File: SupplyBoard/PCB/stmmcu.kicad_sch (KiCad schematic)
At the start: 15 parts, among them J3 Conn_01x04, SW2 RESET, SW3 SW_SPDT, U1 STM32L031F6Px, Y1 16Mhz

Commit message: Supply Board & Folder Organization
Reorganization of the power supply board components, simplifying the layout to facilitate future debugging and reorganizing some folders and documents, as well as adding the power supply board schematic; in supply board only need to make the routing
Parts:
- Y1: footprint Crystal:Crystal_SMD_0603-4Pin_6.0x3.5mm_HandSoldering -> Crystal:Crystal_SMD_2016-4Pin_2.0x1.6mm
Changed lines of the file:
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@@
 			)
 		)
-		(property "Footprint" "Crystal:Crystal_SMD_0603-4Pin_6.0x3.5mm_HandSoldering"
+		(property "Footprint" "Crystal:Crystal_SMD_2016-4Pin_2.0x1.6mm"
 			(at 40.64 76.2 0)
 			(effects

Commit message: Start the S&CBoard
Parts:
- removed C2, C5: 9pF, Capacitor_SMD:C_0805_2012Metric_Pad1.18x1.45mm_HandSolder, symbol Device:C_Small
- removed Y1: 16Mhz, Crystal:Crystal_SMD_2016-4Pin_2.0x1.6mm, symbol Device:Crystal_GND24
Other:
- note removed: "Crystal Osc"
- moved on the sheet: C3, C4

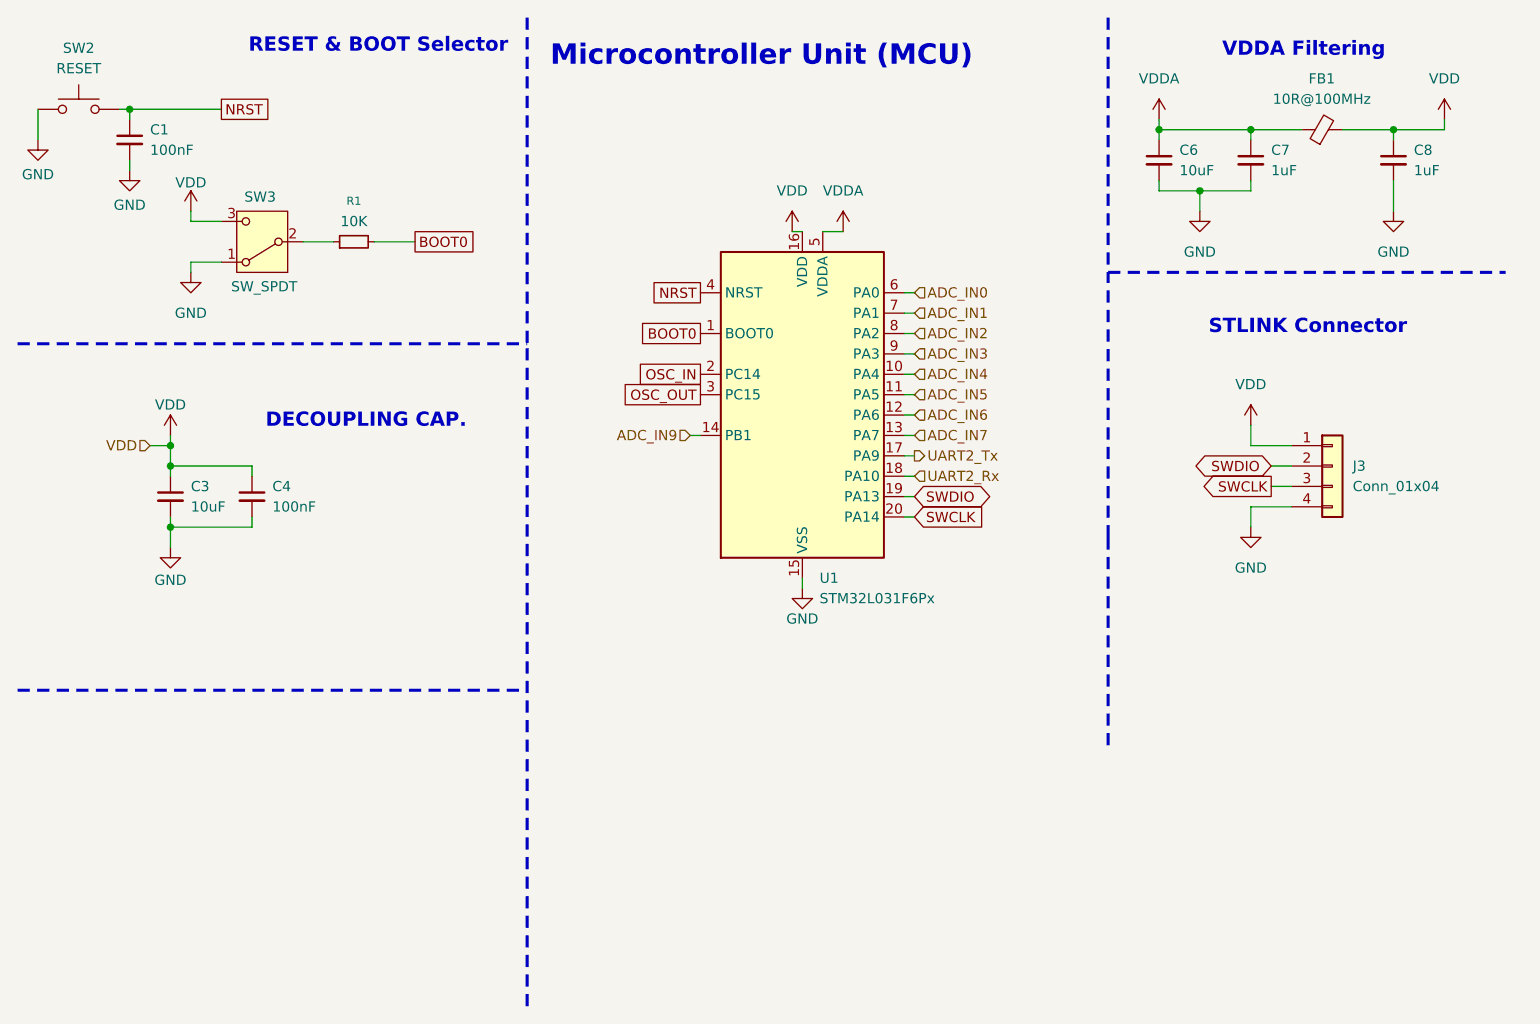
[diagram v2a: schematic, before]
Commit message: Supply & Coms-Sensor Board
la organizacion de los componentes presentes en las placas, se quedaran de esa manera, se espera que en la serigrafia se incluyan los logos de los patrocinadores, ademas se incluyo la carpeta 3D la cual contiene modelos en 3D de las dos placas, con serigrafia y componentes incluidos y ya
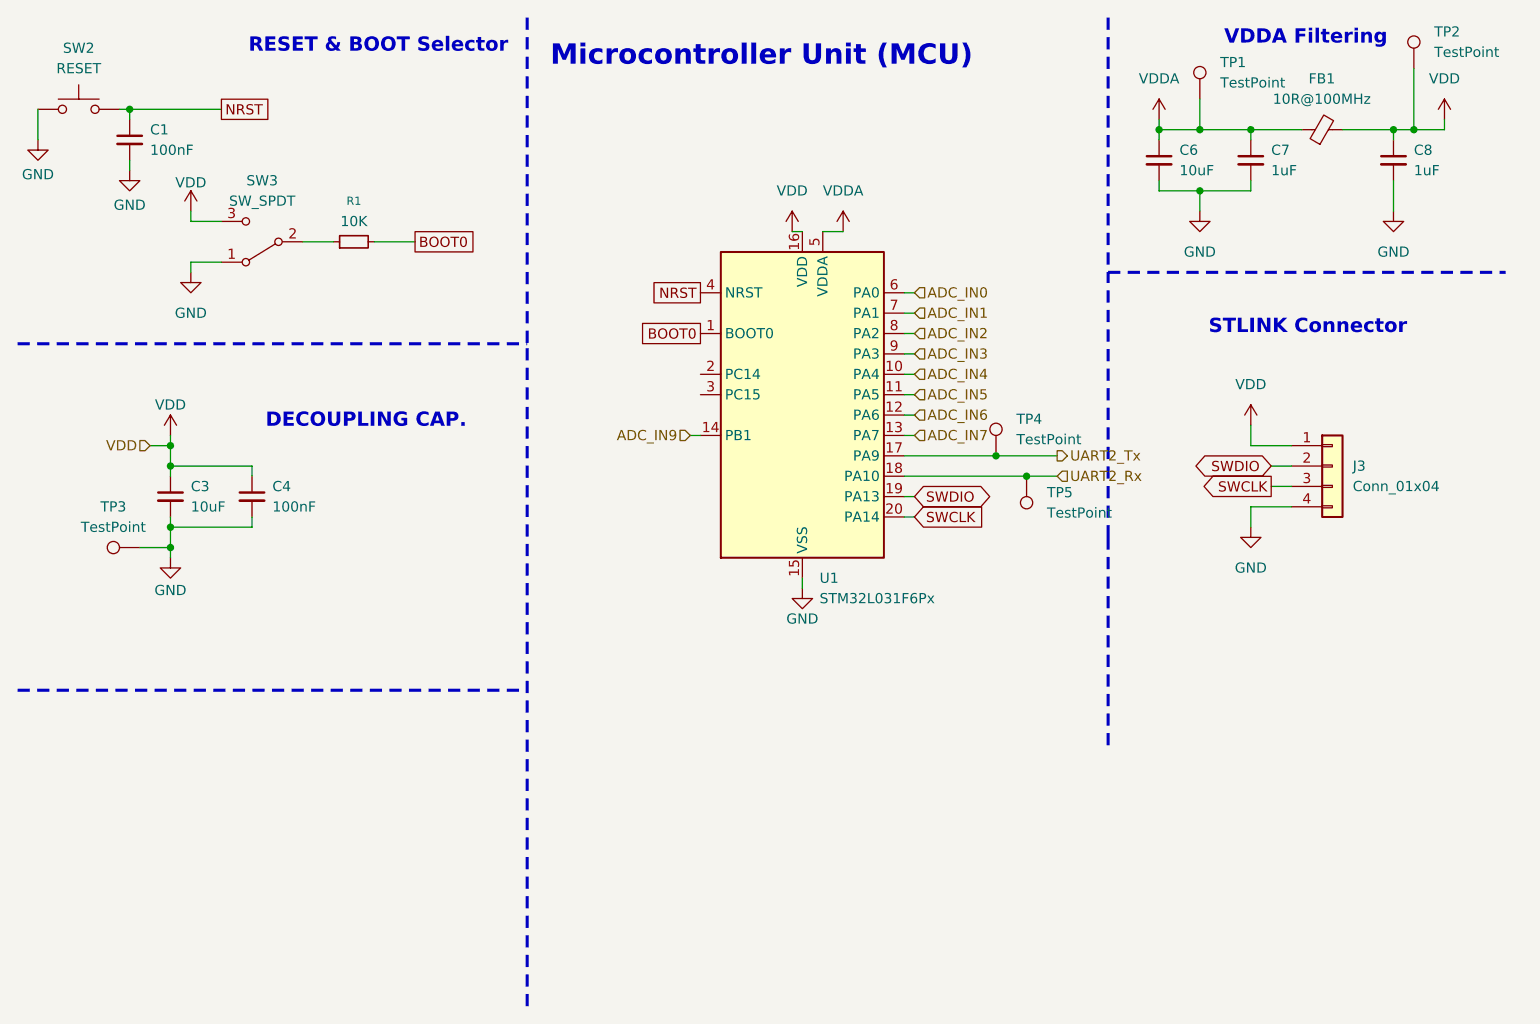
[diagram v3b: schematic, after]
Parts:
- removed SW3: SW_SPDT, Connector_PinHeader_2.54mm:PinHeader_1x03_P2.54mm_Vertical, symbol Switch:SW_SPDT
- added SW3: SW_SPDT, Button_Switch_SMD:SW_SPDT_Shouhan_MSK12C02, symbol CompVuelo:SW_SPDT
- added TP1, TP2, TP3, TP4, TP5: TestPoint, TestPoint:TestPoint_Pad_D1.5mm, symbol Connector:TestPoint
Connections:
- net GND: now also SW3.1, TP3.1
- net UART2_Rx: now also TP5.1
- net UART2_Tx: now also TP4.1
- net VDD: now also SW3.3, TP2.1
- net VDDA: now also TP1.1
- net at R1.1: now also SW3.2
- net OSC_IN: no longer names the net of U1.2 (PC14)
- net OSC_OUT: no longer names the net of U1.3 (PC15)
